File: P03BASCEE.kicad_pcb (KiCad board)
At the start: 2 copper layers, 17 parts, among them J1 Serial, J2 Digital, J3 ICSP, J4 I2C, U1 24LC1025, U2 24LC1025, U3 DS13375+, U4 ATMEGA328P-AU, Y1 Crystal 32MHz, Y2 Crystal 16MHz

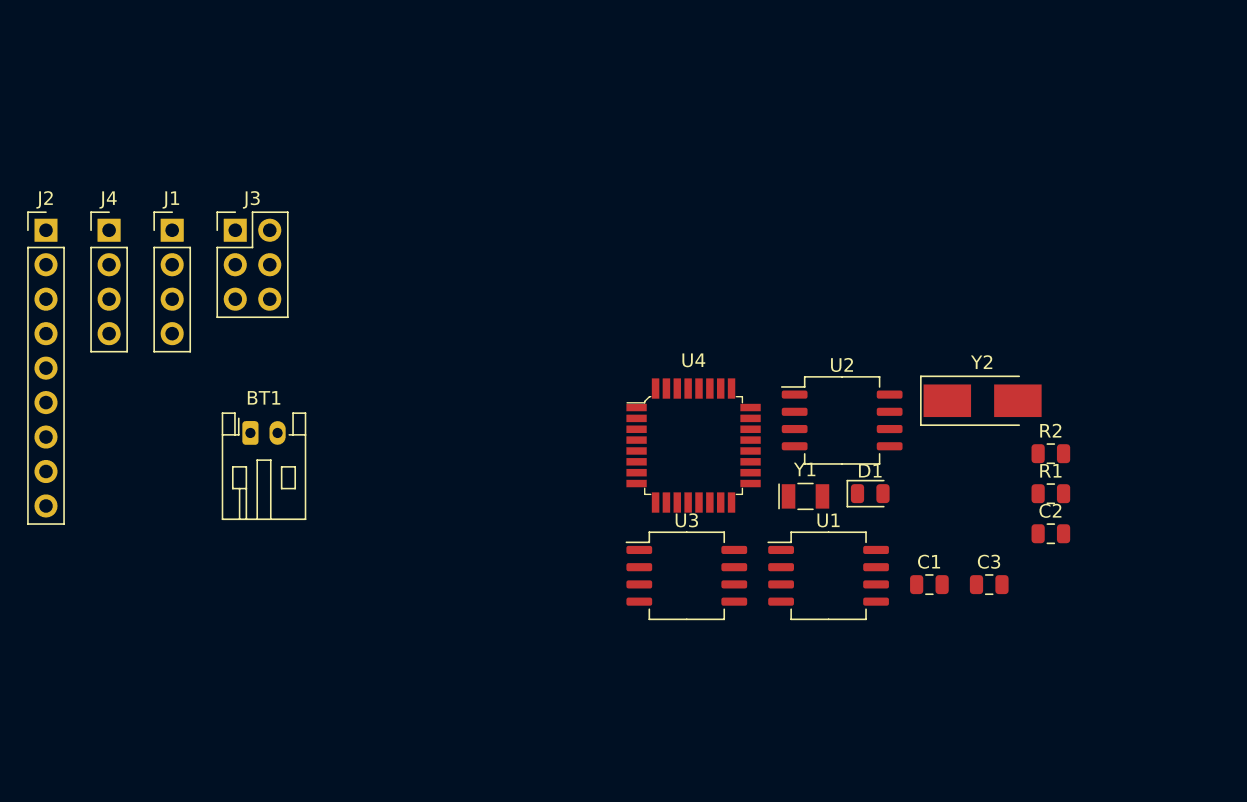
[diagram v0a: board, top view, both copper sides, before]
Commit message: Furos de parafuso adicionados no esquemático e no PCB (boa prática)
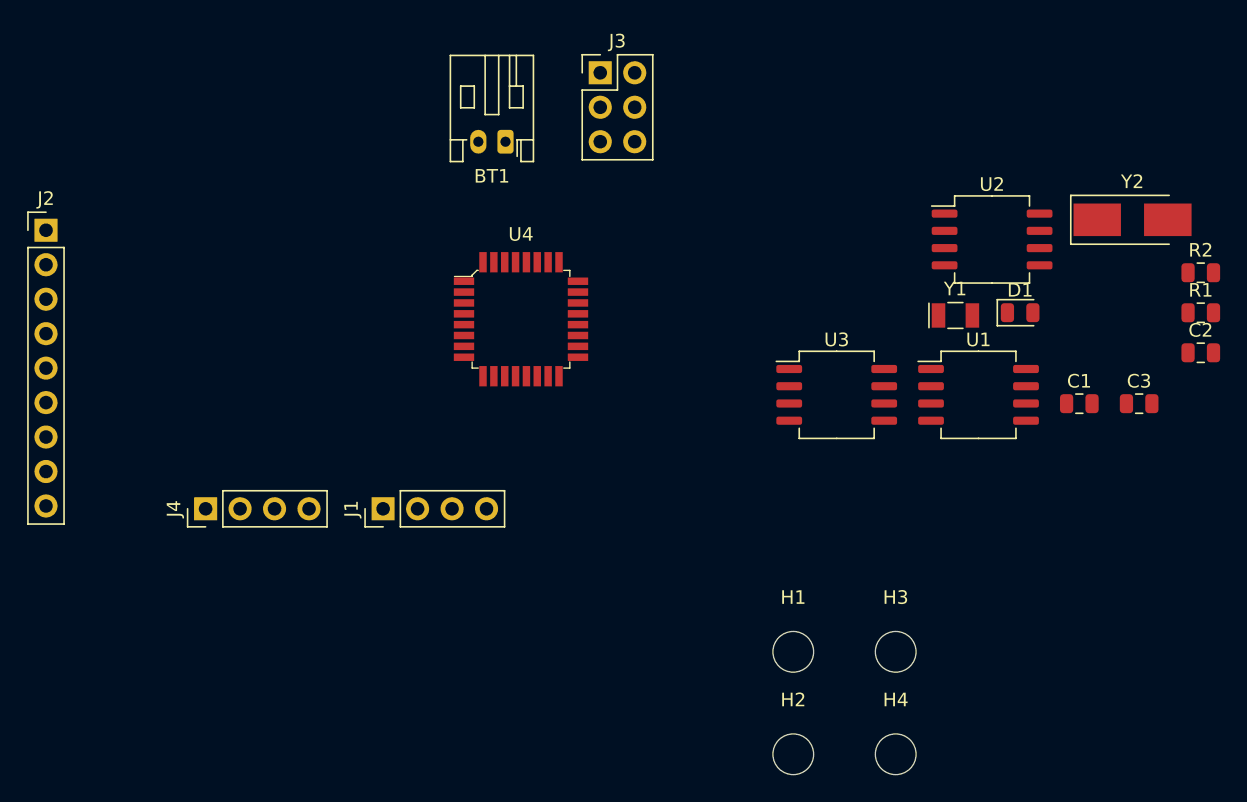
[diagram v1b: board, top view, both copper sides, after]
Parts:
- added H1: MountingHole, MountingHole:MountingHole_3mm, F.Cu at (167.8, 134.0)
- added H2: MountingHole, MountingHole:MountingHole_3mm, F.Cu at (167.8, 141.5)
- added H3: MountingHole, MountingHole:MountingHole_3mm, F.Cu at (175.3, 134.0)
- added H4: MountingHole, MountingHole:MountingHole_3mm, F.Cu at (175.3, 141.5)
- moved J3 29.3 mm to (153.5, 91.3)
- moved BT1 28.5 mm to (146.6, 96.4), turned to 180 degrees
- moved J1 25.7 mm to (137.5, 123.4), turned to 90 degrees
- moved J4 21.7 mm to (124.5, 123.4), turned to 90 degrees
- moved C1 17.3 mm to (188.8, 115.7)
- moved C3 17.3 mm to (193.3, 115.7)
- moved R1 17.3 mm to (197.8, 109.0)
- moved R2 17.3 mm to (197.8, 106.0)
- moved U1 17.3 mm to (181.4, 115.0)
- moved C2 17.3 mm to (197.8, 111.9)
- moved D1 17.3 mm to (184.5, 109.0)
- moved U2 17.3 mm to (182.4, 103.6)
- moved Y2 17.3 mm to (192.8, 102.1)
- moved U3 17.3 mm to (171.0, 115.0)
- moved Y1 17.3 mm to (179.7, 109.2)
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
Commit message: Componentes ajustados de forma compacta na PCB
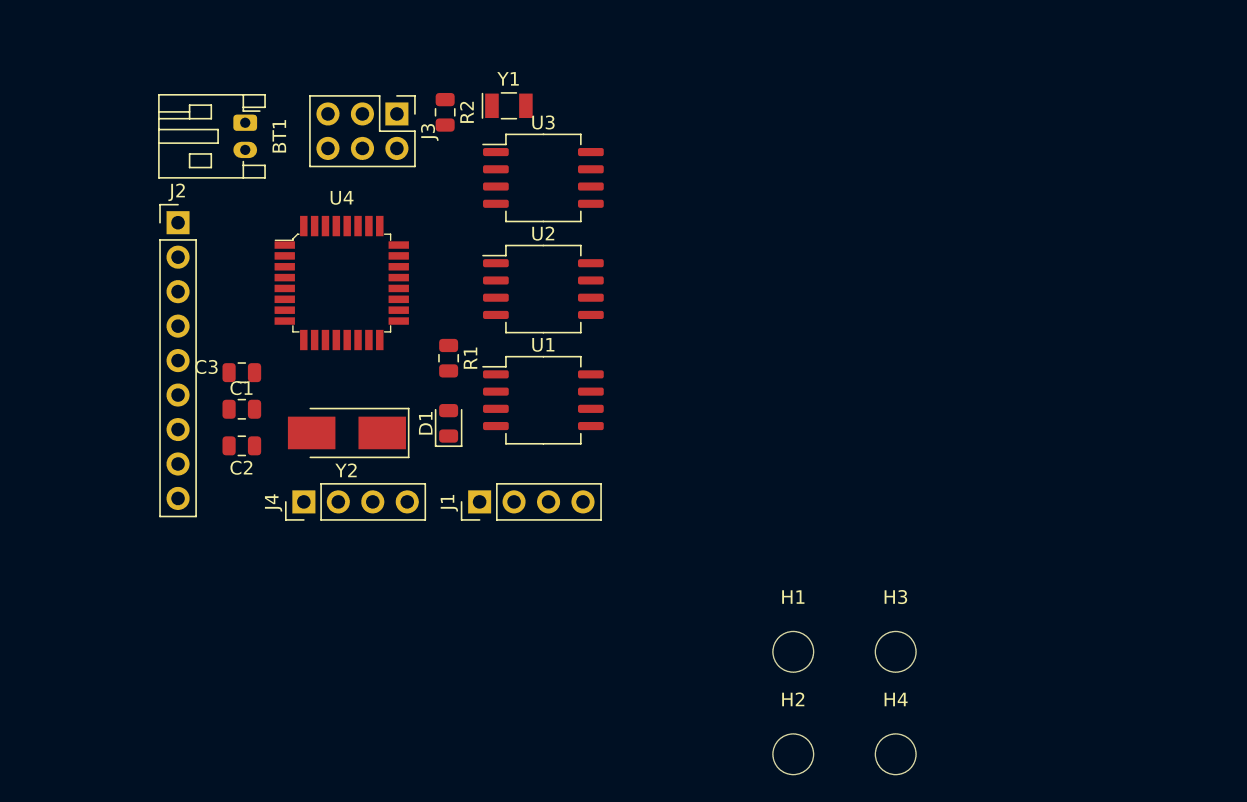
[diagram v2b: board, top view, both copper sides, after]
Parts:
- moved C2 71.0 mm to (127.1, 118.8), turned to 180 degrees
- moved C3 66.2 mm to (127.1, 113.4)
- moved C1 61.7 mm to (127.1, 116.1), turned to 180 degrees
- moved Y2 60.0 mm to (134.9, 117.9), turned to 180 degrees
- moved R2 56.9 mm to (142.1, 94.2), turned to 270 degrees
- moved R1 55.5 mm to (142.4, 112.3), turned to 270 degrees
- moved D1 42.9 mm to (142.4, 117.1), turned to 90 degrees
- moved Y1 36.4 mm to (146.8, 93.7)
- moved U2 33.3 mm to (149.4, 107.3)
- moved U1 32.1 mm to (149.4, 115.4)
- moved U3 26.9 mm to (149.4, 99.1)
- moved BT1 19.2 mm to (127.4, 95.0), turned to 270 degrees
- moved J3 15.3 mm to (138.6, 94.3), turned to 270 degrees
- moved U4 13.5 mm to (134.5, 106.8)
- moved J2 9.75 mm to (122.4, 102.4)
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
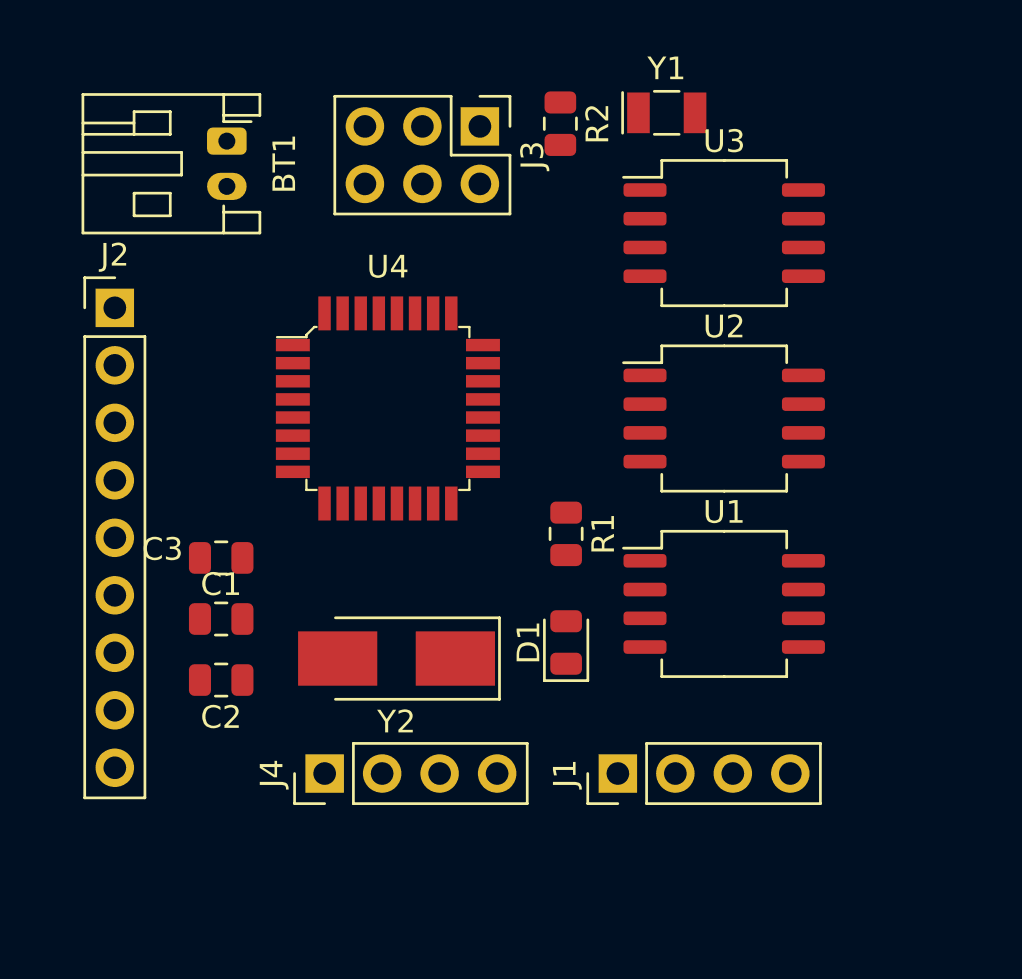
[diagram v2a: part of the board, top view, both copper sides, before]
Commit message: Criada borda da placa - sem espaço para buracos de montage
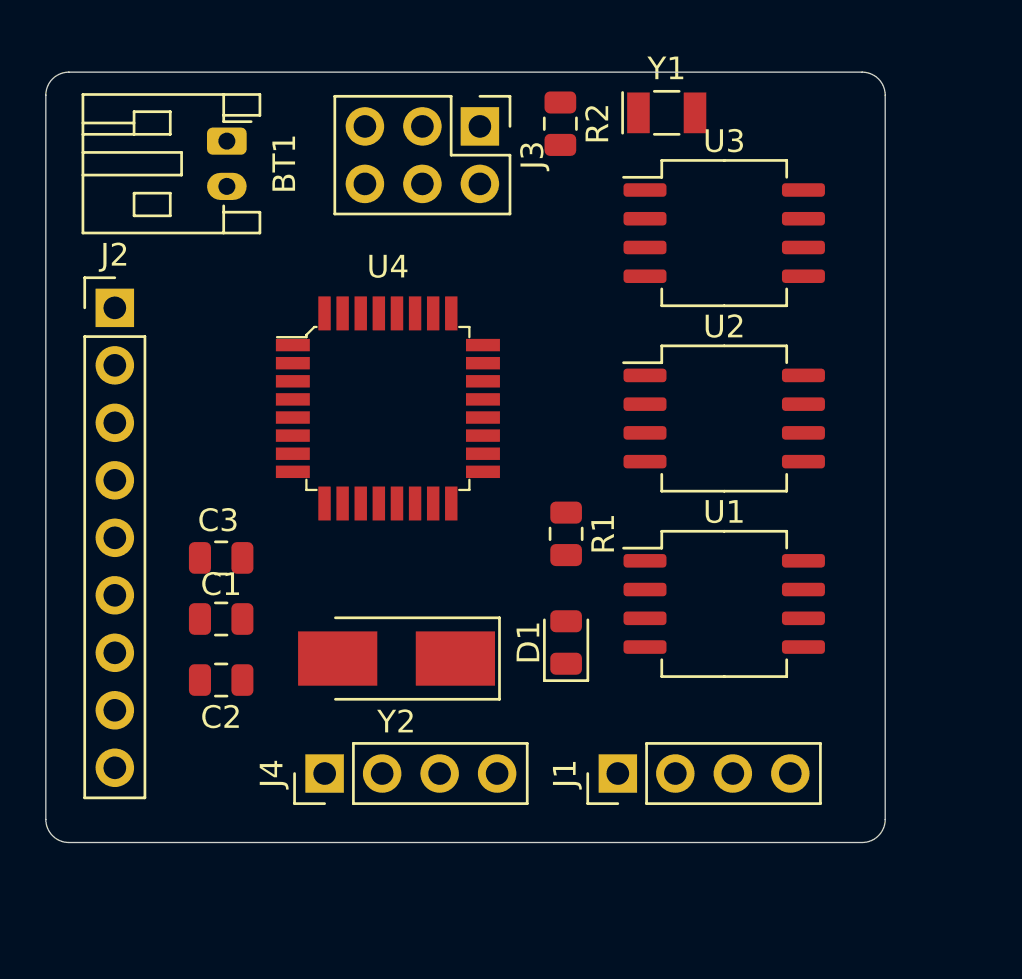
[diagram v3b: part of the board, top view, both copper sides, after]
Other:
- board outline added: 37.1 x 34 mm
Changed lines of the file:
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@@
   (general
     (thickness 1.6)
-    (drawings 0)
+    (drawings 8)
     (tracks 0)
     (zones 0)
@@
     (tags capacitor)
     (attr smd)
-    (fp_text reference C3 (at -2.5885 -0.381 180) (layer F.SilkS)
+    (fp_text reference C3 (at -0.127 -1.651 180) (layer F.SilkS)
       (effects (font (size 1 1) (thickness 0.15)))
     )
@@
     )
   )
+  (gr_arc (start 155.448 92.964) (end 156.464 92.964) (angle -90) (layer Edge.Cuts) (width 0.05))
+  (gr_arc (start 155.448 124.968) (end 155.448 125.984) (angle -90) (layer Edge.Cuts) (width 0.05))
+  (gr_arc (start 120.396 124.968) (end 119.38 124.968) (angle -90) (layer Edge.Cuts) (width 0.05))
+  (gr_arc (start 120.396 92.964) (end 120.396 91.948) (angle -90) (layer Edge.Cuts) (width 0.05))
+  (gr_line (start 119.38 124.968) (end 119.38 92.964) (layer Edge.Cuts) (width 0.05))
+  (gr_line (start 155.448 125.984) (end 120.396 125.984) (layer Edge.Cuts) (width 0.05))
+  (gr_line (start 156.464 92.964) (end 156.464 124.968) (layer Edge.Cuts) (width 0.05))
+  (gr_line (start 120.396 91.948) (end 155.448 91.948) (layer Edge.Cuts) (width 0.05))
 )

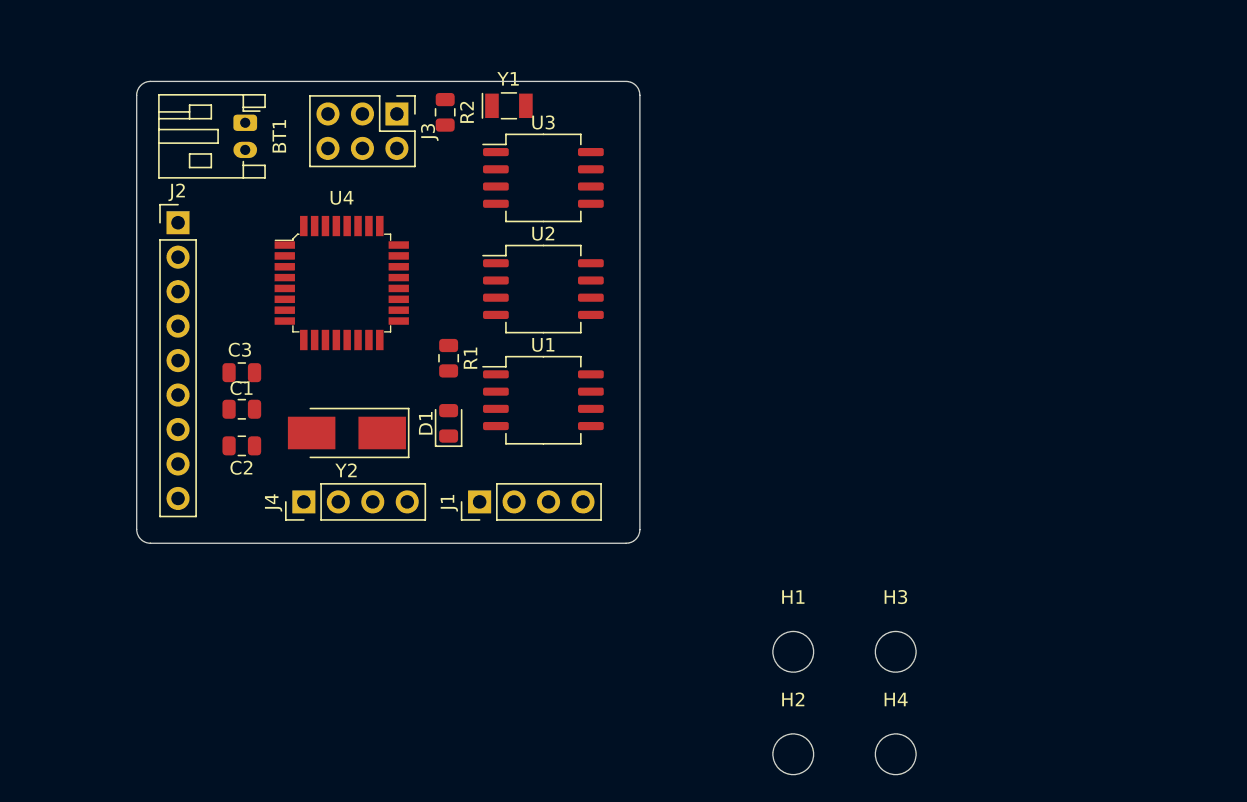
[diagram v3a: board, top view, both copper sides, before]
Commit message: Criada borda da placa - buracos de montagem reduzidos para 2.2mm e incluídos
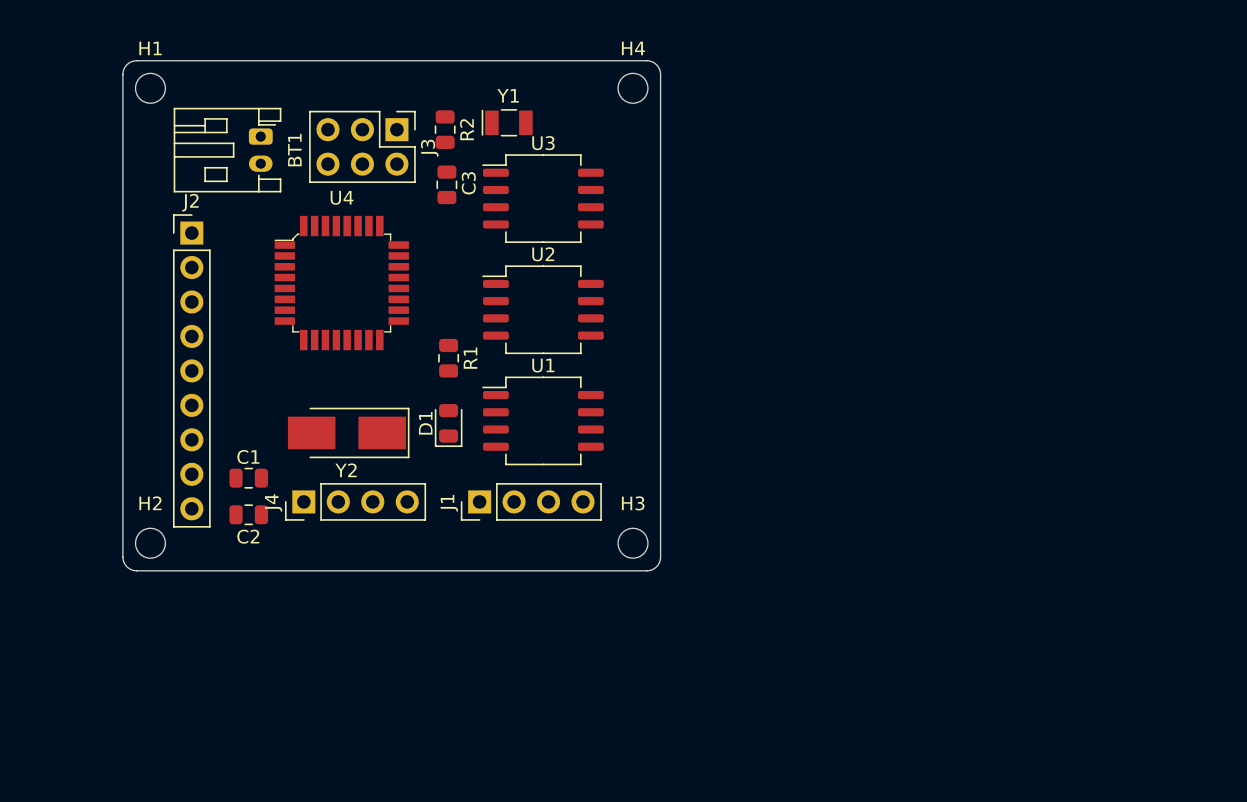
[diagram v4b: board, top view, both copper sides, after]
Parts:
- H1, H2, H3, H4: footprint MountingHole:MountingHole_3mm -> MountingHole:MountingHole_2.2mm_M2_DIN965
- moved H1 63.0 mm to (120.4, 92.5)
- moved H4 52.8 mm to (156.0, 92.5)
- moved H2 49.9 mm to (120.4, 126.0)
- moved H3 20.9 mm to (156.0, 126.0)
- moved C3 20.5 mm to (142.2, 99.6), turned to 270 degrees
- moved C1 5.11 mm to (127.6, 121.2)
- moved C2 5.11 mm to (127.6, 123.9)
- moved BT1 1.53 mm to (128.5, 96.0)
- moved U1 1.52 mm to (149.4, 117.0)
- moved U2 1.52 mm to (149.4, 108.8)
- moved U3 1.52 mm to (149.4, 100.6)
- moved R2 1.28 mm to (142.1, 95.5)
- moved J2 1.27 mm to (123.4, 103.1)
- moved Y1 1.25 mm to (146.8, 95.0)
- moved J3 1.16 mm to (138.6, 95.5)
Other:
- board size 37.1 x 34 mm -> 39.6 x 37.6 mm
